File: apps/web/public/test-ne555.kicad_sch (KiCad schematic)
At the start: 9 parts, among them J1 PWR_5V, U1 NE555P

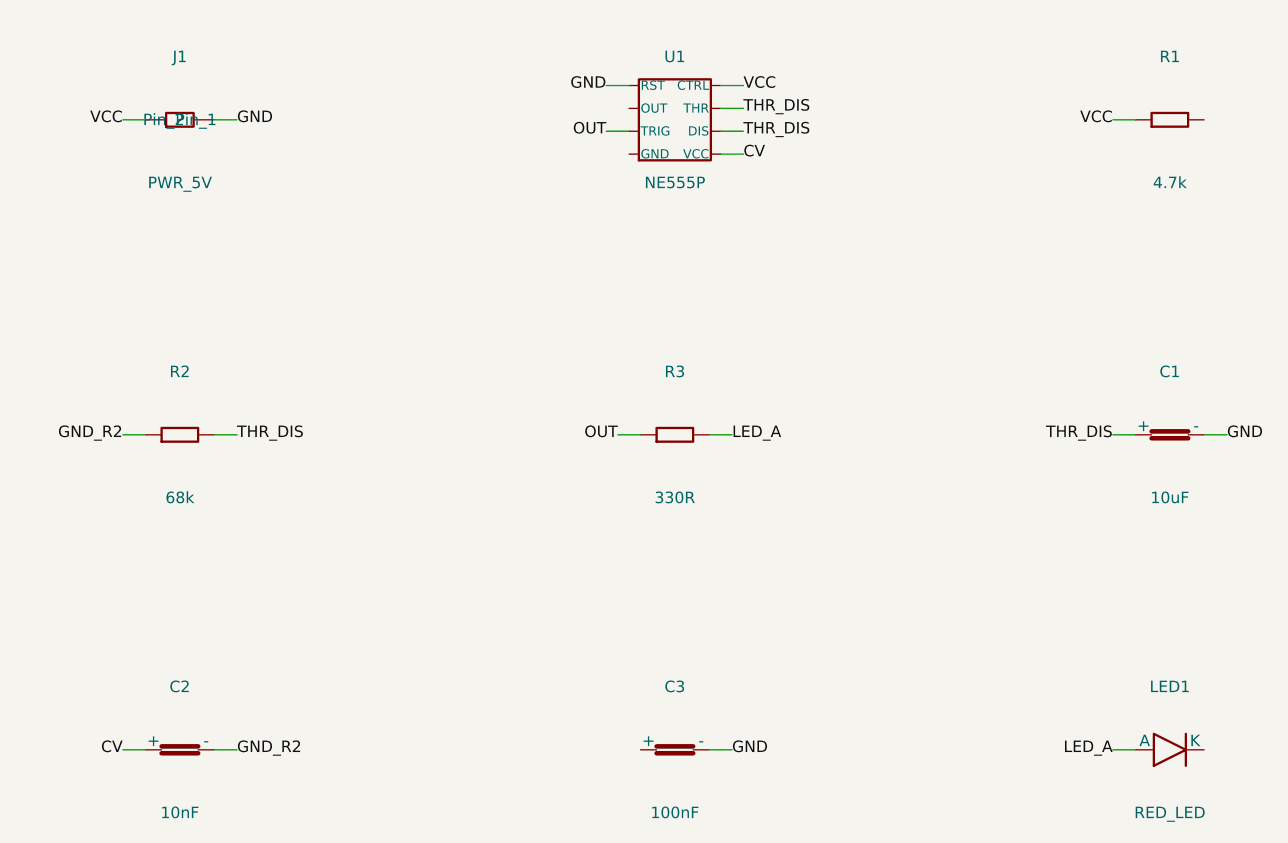
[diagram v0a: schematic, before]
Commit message: fix: remove title_h padding to eliminate empty space at bottom of schematic
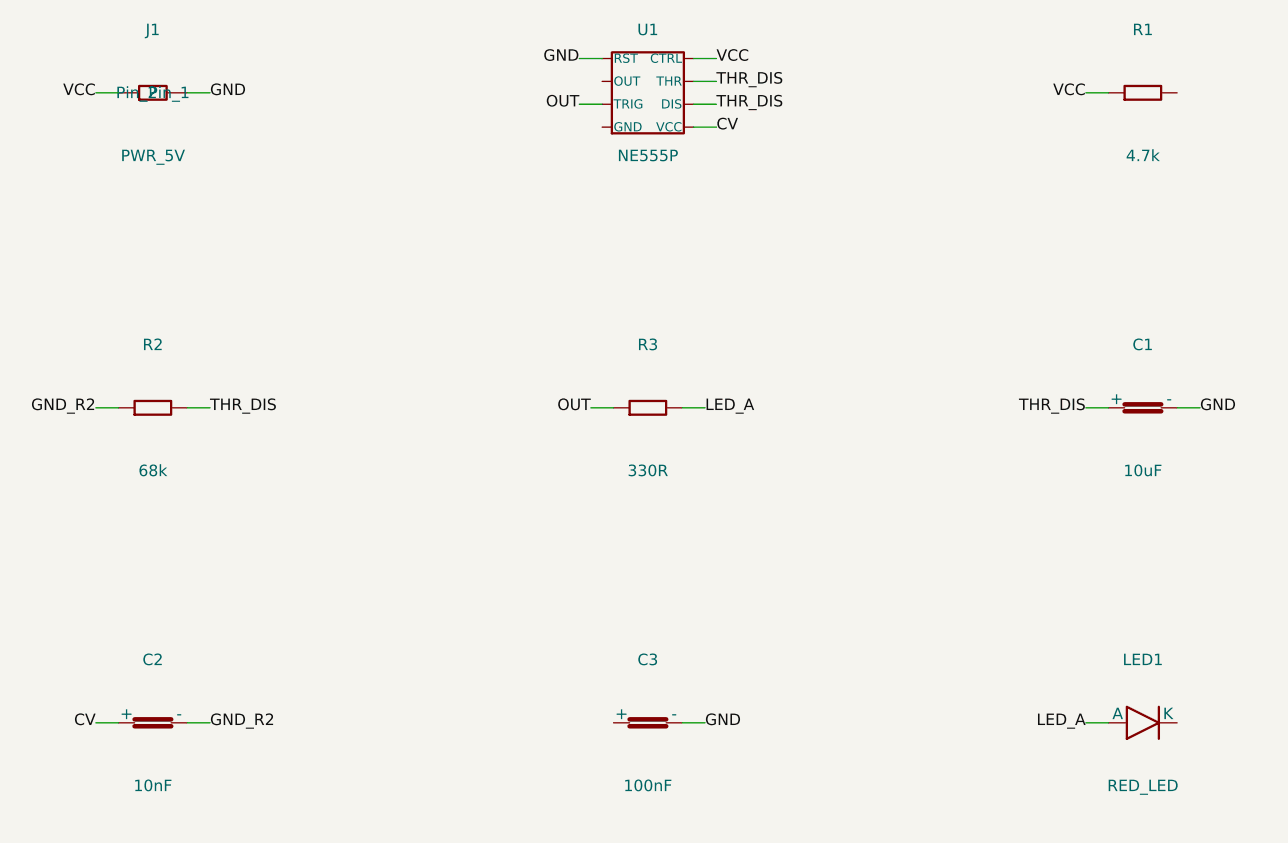
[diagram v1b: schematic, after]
